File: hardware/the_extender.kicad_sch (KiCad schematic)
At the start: 119 parts, among them J0 U262-241N-4BV60, J1 USB_C_Receptacle_USB2.0, J2 U231-091N-3BLRC11, J3 PJ-3136-B, J4 PJ-3136-B, J5 AF 10.0 HC6.3, Q1 SSM3J332R,LF, Q2 SSM3J332R,LF, Q3 Q_PNP_CBE, Q4 SSM3J332R,LF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

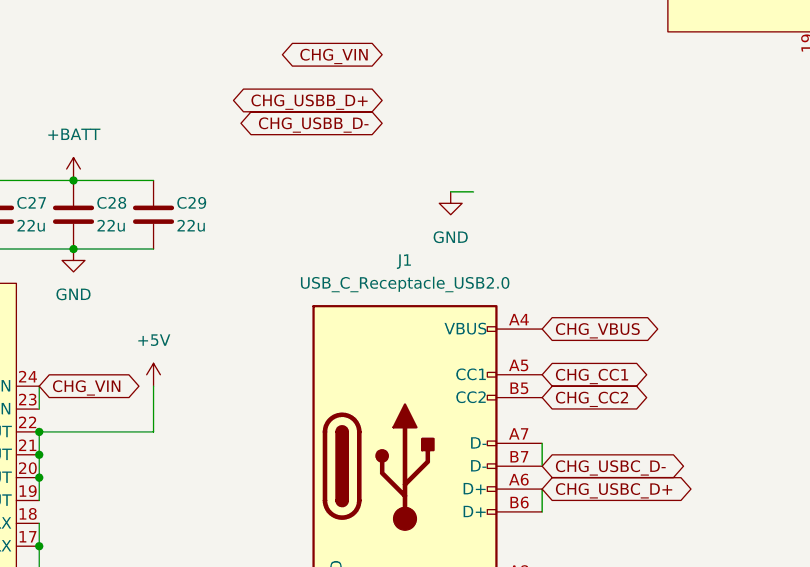
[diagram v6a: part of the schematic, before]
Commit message: add lcsc mappings
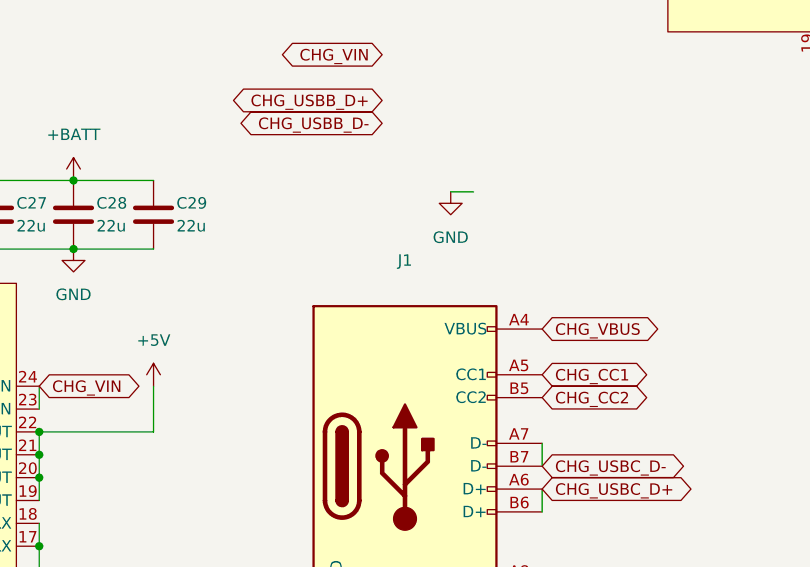
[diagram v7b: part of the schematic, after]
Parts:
- J1: value USB_C_Receptacle_USB2.0 -> (none); footprint e2k_edit:USB-C-SMD_TYPE-C-6PIN-2MD-073 -> (none)
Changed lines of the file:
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@@
     (in_bom yes) (on_board yes)
     (property "Reference" "J1" (id 0) (at 284.48 181.61 0))
-    (property "Value" "USB_C_Receptacle_USB2.0" (id 1) (at 284.48 184.15 0))
-    (property "Footprint" "e2k_edit:USB-C-SMD_TYPE-C-6PIN-2MD-073" (id 2) (at 288.29 204.47 0)
+    (property "Value" "" (id 1) (at 284.48 184.15 0))
+    (property "Footprint" "" (id 2) (at 288.29 204.47 0)
       (effects (font (size 1.27 1.27)) hide)
     )
@@
     )
     (path "/99b3fd77-da13-4321-b5b1-c8bab6e7cb60"
-      (reference "J1") (unit 1) (value "USB_C_Receptacle_USB2.0") (footprint "e2k_edit:USB-C-SMD_TYPE-C-6PIN-2MD-073")
+      (reference "J1") (unit 1) (value "USB-TYPE-C-010") (footprint "e2k_edit:USB-C-SMD_TYPE-C-6PIN-2MD-073")
     )
     (path "/efed6990-d25b-40a3-a7a9-8cc09ff732e7"

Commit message: reread IP5310 datasheet, better groundplanes, other
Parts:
- removed R34: 4k7, Resistor_SMD:R_0805_2012Metric_Pad1.20x1.40mm_HandSolder, symbol Device:R
- J1: value (none) -> USB-TYPE-C-010; footprint (none) -> e2k_edit:USB-C-SMD_TYPE-C-6PIN-2MD-073
- Q3: value Q_PNP_CBE -> MMBT3906LT1G
- U1: value IP5310 -> (none)
- U6: value (none) -> HS-100B; footprint (none) -> Package_QFP:LQFP-48_7x7mm_P0.5mm
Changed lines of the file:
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@@
   (junction (at 243.84 200.66) (diameter 0) (color 0 0 0 0)
   )
-  (junction (at 175.26 181.61) (diameter 0) (color 0 0 0 0)
-  )
   (junction (at 327.66 57.15) (diameter 0) (color 0 0 0 0)
   )
@@
     (stroke (width 0) (type default) (color 0 0 0 0))
   )
-  (wire (pts (xy 167.64 181.61) (xy 175.26 181.61))
-    (stroke (width 0) (type default) (color 0 0 0 0))
-  )
   (wire (pts (xy 99.06 77.47) (xy 124.46 77.47))
     (stroke (width 0) (type default) (color 0 0 0 0))
@@
     )
   )
-  (global_label "PB_INT" (shape input) (at 167.64 189.23 270) (fields_autoplaced)
-    (effects (font (size 1.27 1.27)) (justify right))
-    (property "Intersheet References" "${INTERSHEET_REFS}" (id 0) (at 167.5606 198.0536 90)
-      (effects (font (size 1.27 1.27)) (justify right) hide)
-    )
-  )
   (global_label "MCU_LED" (shape input) (at 74.93 212.09 90) (fields_autoplaced)
     (effects (font (size 1.27 1.27)) (justify left))
@@
     (in_bom yes) (on_board yes)
     (property "Reference" "U1" (id 0) (at 222.25 203.2 0))
-    (property "Value" "IP5310" (id 1) (at 222.25 205.74 0))
+    (property "Value" "" (id 1) (at 222.25 205.74 0))
     (property "Footprint" "Package_DFN_QFN:QFN-32-1EP_5x5mm_P0.5mm_EP3.45x3.45mm" (id 2) (at 222.25 234.95 0)
       (effects (font (size 1.27 1.27)) hide)
@@
     (in_bom yes) (on_board no)
     (property "Reference" "U6" (id 0) (at 59.69 163.83 0))
-    (property "Value" "" (id 1) (at 59.69 166.37 0))
-    (property "Footprint" "" (id 2) (at 59.69 200.66 0)
+    (property "Value" "HS-100B" (id 1) (at 59.69 166.37 0))
+    (property "Footprint" "Package_QFP:LQFP-48_7x7mm_P0.5mm" (id 2) (at 59.69 200.66 0)
       (effects (font (size 1.27 1.27)) hide)
     )
@@
     (in_bom yes) (on_board yes)
     (property "Reference" "J1" (id 0) (at 284.48 181.61 0))
-    (property "Value" "" (id 1) (at 284.48 184.15 0))
-    (property "Footprint" "" (id 2) (at 288.29 204.47 0)
+    (property "Value" "USB-TYPE-C-010" (id 1) (at 284.48 184.15 0))
+    (property "Footprint" "e2k_edit:USB-C-SMD_TYPE-C-6PIN-2MD-073" (id 2) (at 288.29 204.47 0)
       (effects (font (size 1.27 1.27)) hide)
     )
@@
     (in_bom yes) (on_board yes)
     (property "Reference" "Q3" (id 0) (at 171.45 251.46 90))
-    (property "Value" "Q_PNP_CBE" (id 1) (at 171.45 254 90))
+    (property "Value" "MMBT3906LT1G" (id 1) (at 171.45 254 90))
     (property "Footprint" "Package_TO_SOT_SMD:SOT-23_Handsoldering" (id 2) (at 173.99 254 0)
       (effects (font (size 1.27 1.27)) hide)
@@
     (pin "1")
   )
-  (symbol (lib_id "Device:R") (at 167.64 185.42 0) (unit 1)
-    (in_bom yes) (on_board yes)
-    (property "Reference" "R34" (id 0) (at 165.1 186.69 90)
-      (effects (font (size 1.27 1.27)) (justify left))
-    )
-    (property "Value" "4k7" (id 1) (at 167.64 186.69 90)
-      (effects (font (size 1.27 1.27)) (justify left))
-    )
-    (property "Footprint" "Resistor_SMD:R_0805_2012Metric_Pad1.20x1.40mm_HandSolder" (id 2) (at 165.862 185.42 90)
-      (effects (font (size 1.27 1.27)) hide)
-    )
-    (property "Datasheet" "~" (id 3) (at 167.64 185.42 0)
-      (effects (font (size 1.27 1.27)) hide)
-    )
-    (pin "1")
-    (pin "2")
-  )
   (symbol (lib_id "Device:R") (at 381 67.31 90) (unit 1)
     (in_bom yes) (on_board yes)
@@
     )
     (path "/aef19f89-9756-4d85-a211-34cb4173f807"
-      (reference "Q3") (unit 1) (value "Q_PNP_CBE") (footprint "Package_TO_SOT_SMD:SOT-23_Handsoldering")
+      (reference "Q3") (unit 1) (value "MMBT3906LT1G") (footprint "Package_TO_SOT_SMD:SOT-23_Handsoldering")
     )
     (path "/c8fdf199-8ec8-4926-963e-b0e207fb17a3"
@@
       (reference "R33") (unit 1) (value "10k") (footprint "Resistor_SMD:R_0805_2012Metric_Pad1.20x1.40mm_HandSolder")
     )
-    (path "/e6e84f42-dc69-4e44-9e0c-06d99eedd7ef"
-      (reference "R34") (unit 1) (value "4k7") (footprint "Resistor_SMD:R_0805_2012Metric_Pad1.20x1.40mm_HandSolder")
-    )
     (path "/67800f9e-414e-49be-af4c-0f14dddef3de"
       (reference "TH1") (unit 1) (value "R100k B4100") (footprint "Resistor_SMD:R_0805_2012Metric_Pad1.20x1.40mm_HandSolder")
@@
     )
     (path "/4ca92096-0499-4734-8620-6a654dac35e8"
-      (reference "U1") (unit 1) (value "IP5310") (footprint "Package_DFN_QFN:QFN-32-1EP_5x5mm_P0.5mm_EP3.45x3.45mm")
+      (reference "U1") (unit 1) (value "IP5310-I2C") (footprint "Package_DFN_QFN:QFN-32-1EP_5x5mm_P0.5mm_EP3.45x3.45mm")
     )
     (path "/44fd8df2-cc1a-47a1-b6cc-08af9e746772"
